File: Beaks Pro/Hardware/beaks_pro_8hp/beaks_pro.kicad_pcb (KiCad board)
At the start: 2 copper layers, 40 x 110 mm, 138 parts, among them J1 Pins_02x10_P2.54mm_TH, J11 out1, J12 out2, J13 Eurorack Power, J14 Pins_02x10_P2.54mm_TH, J2 Pins_02x10_P2.54mm_TH, J3 CV1, J4 CV2, J5 CV3, J6 CV4, J7 in1, J8 in2, J9 Pins_02x10_P2.54mm_TH, Q1 2N3904, Q2 2N3904, SW2 SW_Dual, SW3 SW_Mode, SW5 SW_ML6, SW6 SW_ML6, U1 TL072CP, U2 MCP6002-I-P, U3 TL072CP, U4 MCP6002-I-P, U5 TL074, U6 LM4040LP-10, U7 L78L05_TO92, U8 Bluepill, U9 TL072CP

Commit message: Layout done on 8HP SMT version
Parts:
- removed D10: 3.6, Diode_THT:D_DO-35_SOD27_P7.62mm_Horizontal
- added C25: 100n, Capacitor_SMD:C_0603_1608Metric_Pad1.08x0.95mm_HandSolder, F.Cu at (170.5, 74.0)
- added C26: 100n, Capacitor_SMD:C_0603_1608Metric_Pad1.08x0.95mm_HandSolder, F.Cu at (187.5, 101.4)
- added DZ1: ZMM3V6, PCM_Diode_SMD_AKL:D_SOD-323, F.Cu at (154.0, 138.0)
- C1, C13, C16, C2, C20, C22, C24, C5, C6: footprint Capacitor_THT:C_Rect_L10.0mm_W4.0mm_P7.50mm_MKS4 -> Capacitor_SMD:C_0603_1608Metric_Pad1.08x0.95mm_HandSolder
- C10, C11, C12, C14, C15, C3, C4, C7, C8, C9: footprint Capacitor_THT:C_Disc_D3.4mm_W2.1mm_P2.50mm -> Capacitor_SMD:C_0603_1608Metric_Pad1.08x0.95mm_HandSolder
- C17, C18, C19: value 10u -> 22uF; footprint Capacitor_THT:CP_Radial_D8.0mm_P3.50mm -> Capacitor_SMD:C_1206_3216Metric_Pad1.33x1.80mm_HandSolder
- C21: value 0,33u -> 22uF; footprint Capacitor_THT:C_Rect_L10.0mm_W4.0mm_P7.50mm_MKS4 -> Capacitor_SMD:C_1206_3216Metric_Pad1.33x1.80mm_HandSolder
- C23: value 100n -> 22uF; footprint Capacitor_THT:C_Rect_L10.0mm_W4.0mm_P7.50mm_MKS4 -> Capacitor_SMD:C_1206_3216Metric_Pad1.33x1.80mm_HandSolder
- D11, D8, D9: value 1N5817 -> B140HW-7; footprint Diode_THT:D_DO-41_SOD81_P10.16mm_Horizontal -> Diode_SMD:D_SOD-123
- J1: value Pins_02x10_P2.54mm_TH -> Conn_02x08_Odd_Even; footprint Connector_PinHeader_2.54mm:PinHeader_2x10_P2.54mm_Vertical -> Connector_PinSocket_2.54mm:PinSocket_2x08_P2.54mm_Vertical
- J13, U8: moved to B.Cu
- J14: value Pins_02x10_P2.54mm_TH -> Conn_02x12_Odd_Even; footprint Connector_PinHeader_2.54mm:PinHeader_2x10_P2.54mm_Vertical -> Connector_PinSocket_2.54mm:PinSocket_2x12_P2.54mm_Vertical
- J2: value Pins_02x10_P2.54mm_TH -> Conn_02x12_Odd_Even; footprint Connector_PinSocket_2.54mm:PinSocket_2x10_P2.54mm_Vertical -> Connector_PinHeader_2.54mm:PinHeader_2x12_P2.54mm_Vertical
- J9: value Pins_02x10_P2.54mm_TH -> Conn_02x08_Odd_Even; footprint Connector_PinSocket_2.54mm:PinSocket_2x10_P2.54mm_Vertical -> Connector_PinHeader_2.54mm:PinHeader_2x08_P2.54mm_Vertical
- Q1, Q2: value 2N3904 -> S8050 J3Y; footprint Package_TO_SOT_THT:TO-92_Inline_Wide -> PCM_Package_TO_SOT_SMD_AKL:SOT-23
- R1, R10, R11, R12, R13, R14, R15, R16, R17, R18, R19, R2, R20, R21, R22, R23, R24, R25, R26, R27, R28, R29, R3, R30, R31, R32, R33, R34, R35, R36, R37, R38, R39, R4, R40, R41, R42, R43, R44, R45, R46, R47, R48, R49, R5, R50, R51, R52, R53, R54, R55, R56, R57, R58, R59, R6, R60, R61, R62, R63, R64, R65, R7, R8, R9: footprint Resistor_THT:R_Axial_DIN0207_L6.3mm_D2.5mm_P7.62mm_Horizontal -> Resistor_SMD:R_0603_1608Metric_Pad0.98x0.95mm_HandSolder
- U1, U3, U9: value TL072CP -> TL072CD; footprint PCM_Package_DIP_AKL:DIP-8_W7.62mm_Socket_LongPads -> PCM_Package_SO_AKL:SO-8_3.9x4.9mm_P1.27mm
- U2, U4: value MCP6002-I-P -> MCP6002-I-SN; footprint PCM_Package_DIP_AKL:DIP-8_W7.62mm_Socket_LongPads -> PCM_Package_SO_AKL:SO-8_3.9x4.9mm_P1.27mm
- U5: value TL074 -> TL074CD; footprint Package_DIP:DIP-14_W7.62mm_Socket_LongPads -> PCM_Package_SO_AKL:SOIC-14_3.9x8.7mm_P1.27mm
- U6: value LM4040LP-10 -> LM4040DBZ-10; footprint Package_TO_SOT_THT:TO-92_Inline_Wide -> Package_TO_SOT_SMD:SOT-23
- U7: value L78L05_TO92 -> AMS1117-5.0; footprint PCM_Package_TO_SOT_THT_AKL:TO-92L_Inline_Wide -> Package_TO_SOT_SMD:SOT-223-3_TabPin2
- moved H1 381.5 mm to (173.0, 43.5)
- moved C24 345.8 mm to (158.0, 111.0), turned to 90 degrees
- moved J1 344.6 mm to (174.0, 98.0)
- moved U9 342.4 mm to (162.0, 111.5), turned to -90 degrees
- moved J14 341.0 mm to (184.0, 122.5), turned to -90 degrees
- moved R59 336.6 mm to (156.0, 112.0), turned to 90 degrees
- moved R63 336.6 mm to (156.0, 126.6), turned to 180 degrees
- moved R58 335.8 mm to (157.1, 115.0)
- moved R60 335.6 mm to (157.0, 117.0)
- moved R62 333.3 mm to (159.4, 126.6), turned to 180 degrees
- moved R64 333.0 mm to (159.5, 128.6), turned to 180 degrees
- moved R61 332.1 mm to (160.5, 117.0)
- moved R65 329.6 mm to (163.5, 106.5)
- moved R43 325.8 mm to (167.5, 113.0), turned to 180 degrees
- moved R44 325.6 mm to (167.5, 115.0), turned to 180 degrees
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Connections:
- C13 pad 2: -12V -> GND
- C21 pad 1: +12V -> +5V
- C23 pad 1: +5V -> +12V
- C5 pad 2: -12V -> GND
- J1 pad 1: /PRE_ATV_OUT1 -> /LED_SALIDA_1
- J1 pad 10: /SW_TRIG1 -> GND
- J1 pad 11: /LED2 -> /LED4
- J1 pad 12: /SW_TRIG2 -> GND
- J1 pad 13: /LED3 -> /LED5
- J1 pad 14: GND -> /OUT1
- J1 pad 15: /LED4 -> GND
- J1 pad 16: GND -> /OUT2
- J1 pad 2: /PRE_ATV_OUT2 -> /SW_DUAL
- J1 pad 3: /OUT1_ATVPOT -> /LED_SALIDA_2
- J1 pad 4: /OUT2_ATVPOT -> /SW_MODE
- J1 pad 5: /LED_SALIDA_1 -> /LED1
- J1 pad 6: /SW_DUAL -> /SW_TRIG1
- J1 pad 7: /LED_SALIDA_2 -> /LED2
- J1 pad 8: /SW_MODE -> /SW_TRIG2
- J1 pad 9: /LED1 -> /LED3
- J2 pad 1: GND -> GND1
- J2 pad 10: /Front PCB/CV2_JACK -> /Front PCB/TRIG_2
- J2 pad 11: /Front PCB/CV4_POT -> /Front PCB/CV2_ATVPOT
- J2 pad 12: /Front PCB/CV2_ATVPOT -> /Front PCB/CV4_POT
- J2 pad 13: /Front PCB/CV4_ATVPOT -> /Front PCB/CV2_POT
- J2 pad 14: /Front PCB/CV2_POT -> /Front PCB/CV4_ATVPOT
- J2 pad 15: /Front PCB/CV4_JACK -> /Front PCB/CV3_JACK
- J2 pad 16: /Front PCB/CV3_JACK -> /Front PCB/CV4_JACK
- J2 pad 17: /Front PCB/CV3_POT -> /Front PCB/CV3_ATVPOT
- J2 pad 18: /Front PCB/CV3_ATVPOT -> /Front PCB/CV3_POT
- J2 pad 19: GND -> GND1
- J2 pad 2: GND -> GND1
- J2 pad 20: GND -> GND1
- J2 pad 3: /Front PCB/-10V_REF -> /Front PCB/CV1_JACK
- J2 pad 4: /Front PCB/CV1_JACK -> /Front PCB/-10V_REF
- J2 pad 5: GND -> /Front PCB/CV1_ATVPOT
- J2 pad 6: /Front PCB/CV1_ATVPOT -> GND1
- J2 pad 7: /Front PCB/TRIG_1 -> /Front PCB/CV1_POT
- J2 pad 8: /Front PCB/CV1_POT -> /Front PCB/TRIG_1
- J2 pad 9: /Front PCB/TRIG_2 -> /Front PCB/CV2_JACK
- J9 pad 1: /Front PCB/PRE_ATV_OUT2 -> /Front PCB/LED_SALIDA_1
- J9 pad 10: /Front PCB/LED1 -> GND1
- J9 pad 11: /Front PCB/SW_TRIG2 -> /Front PCB/LED4
- J9 pad 12: /Front PCB/LED2 -> GND1
- J9 pad 13: GND -> /Front PCB/LED5
- J9 pad 14: /Front PCB/LED3 -> /Front PCB/OUT1
- J9 pad 15: GND -> GND1
- J9 pad 16: /Front PCB/LED4 -> /Front PCB/OUT2
- J9 pad 2: /Front PCB/PRE_ATV_OUT1 -> /Front PCB/SW_DUAL
- J9 pad 3: /Front PCB/OUT2_ATVPOT -> /Front PCB/LED_SALIDA_2
- J9 pad 4: /Front PCB/OUT1_ATVPOT -> /Front PCB/SW_MODE
- J9 pad 5: /Front PCB/SW_DUAL -> /Front PCB/LED1
- J9 pad 6: /Front PCB/LED_SALIDA_1 -> /Front PCB/SW_TRIG1
- J9 pad 7: /Front PCB/SW_MODE -> /Front PCB/LED2
- J9 pad 8: /Front PCB/LED_SALIDA_2 -> /Front PCB/SW_TRIG2
- J9 pad 9: /Front PCB/SW_TRIG1 -> /Front PCB/LED3
- Q1 pad 1: GND -> Net-(Q1-B)
- Q1 pad 2: Net-(Q1-B) -> GND
- Q2 pad 1: GND -> Net-(Q2-B)
- Q2 pad 2: Net-(Q2-B) -> GND
- U6 pad 1: unconnected-(U6-NC-Pad1) -> GND
- U6 pad 2: GND -> /-10V_REF
- U6 pad 3: /-10V_REF -> unconnected-(U6-NC-Pad3)
- U7 pad 1: +5V -> GND
- U7 pad 2: GND -> +5V
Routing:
- net -12V: track 0.00 -> 284.4 mm, vias 0 -> 6
- net +12V: track 0.00 -> 249.9 mm, vias 0 -> 6
- net /Front PCB/CV1_JACK: track 0.00 -> 164.2 mm
- net /Output/-3V6_REF: track 0.00 -> 148.5 mm, vias 0 -> 3
- net /Front PCB/CV3_ATVPOT: track 0.00 -> 125.7 mm
- net /Front PCB/CV4_JACK: track 0.00 -> 120.9 mm, vias 0 -> 1
- net /PRE_ATV_OUT2: track 0.00 -> 109.2 mm, vias 0 -> 1
- net Net-(U4A--): track 0.00 -> 99.6 mm, vias 0 -> 3
- net +3V3: track 0.00 -> 94.2 mm, vias 0 -> 4
- net /Front PCB/CV4_ATVPOT: track 0.00 -> 94.0 mm
- net /PRE_ATV_OUT1: track 0.00 -> 93.2 mm
- net /Front PCB/CV4_POT: track 0.00 -> 87.7 mm
- net /Front PCB/-10V_REF: track 0.00 -> 87.0 mm
- net /Front PCB/CV3_JACK: track 0.00 -> 83.7 mm
- net Net-(U2A--): track 0.00 -> 80.5 mm, vias 0 -> 2
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- added copper zone on B.Cu, net GND
- added copper zone on F.Cu, net GND
- added copper zone on B.Cu, net GND1
- added copper zone on F.Cu, net GND1
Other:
- board size 40 x 110 mm -> 90 x 110 mm
- board text added: "**"

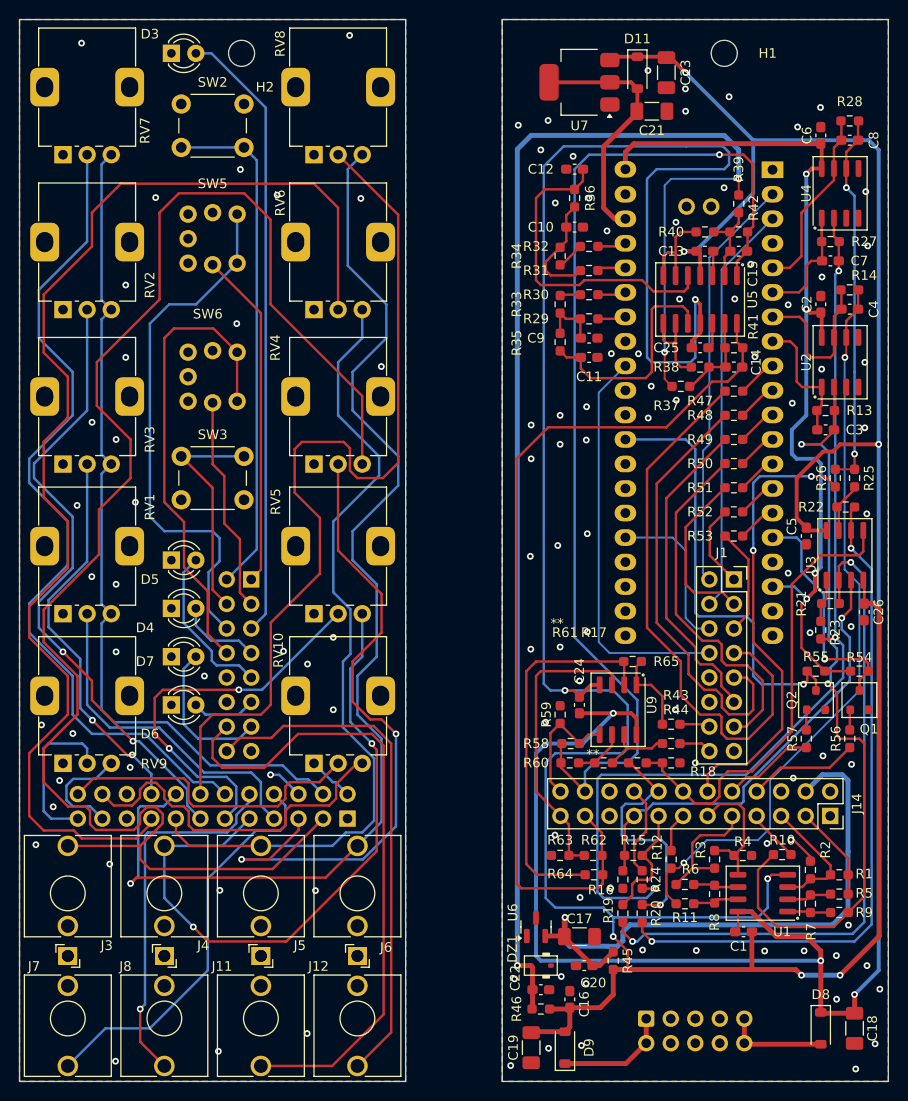
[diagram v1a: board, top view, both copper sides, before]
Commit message: Split 8HP design up in separate files, for SMT export. Add step file export
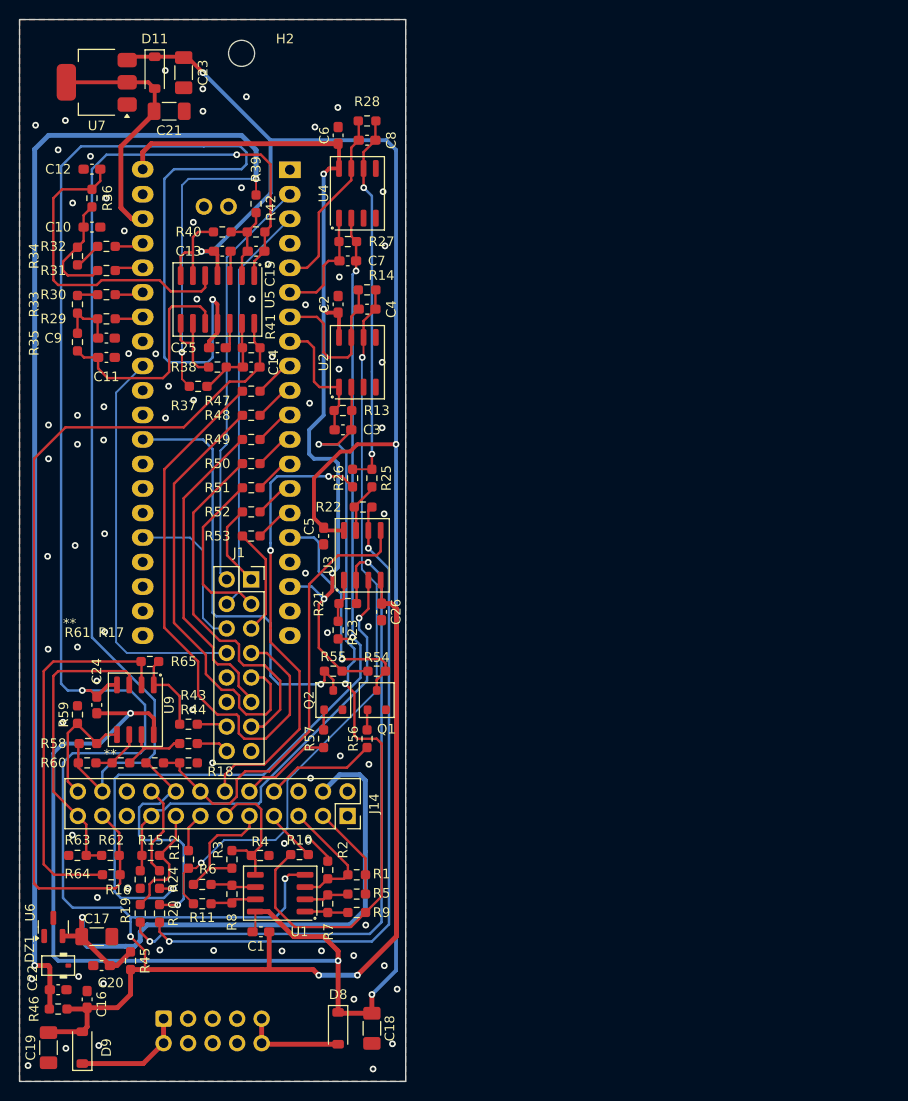
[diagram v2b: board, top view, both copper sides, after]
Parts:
- removed D3, D4, D5, D6, D7: LED, LED_THT:LED_D3.0mm
- removed H1: MountingHole, MountingHole:MountingHole_2.7mm_M2.5
- removed J11: out1, Library:Jack_3.5mm_QingPu_WQP-PJ398SM_Vertical_CircularHoles_3D
- removed J12: out2, Library:Jack_3.5mm_QingPu_WQP-PJ398SM_Vertical_CircularHoles_3D
- removed J2: Conn_02x12_Odd_Even, Connector_PinHeader_2.54mm:PinHeader_2x12_P2.54mm_Vertical
- removed J3: CV1, Library:Jack_3.5mm_QingPu_WQP-PJ398SM_Vertical_CircularHoles_3D
- removed J4: CV2, Library:Jack_3.5mm_QingPu_WQP-PJ398SM_Vertical_CircularHoles_3D
- removed J5: CV3, Library:Jack_3.5mm_QingPu_WQP-PJ398SM_Vertical_CircularHoles_3D
- removed J6: CV4, Library:Jack_3.5mm_QingPu_WQP-PJ398SM_Vertical_CircularHoles_3D
- removed J7: in1, Library:Jack_3.5mm_QingPu_WQP-PJ398SM_Vertical_CircularHoles_3D
- removed J8: in2, Library:Jack_3.5mm_QingPu_WQP-PJ398SM_Vertical_CircularHoles_3D
- removed J9: Conn_02x08_Odd_Even, Connector_PinHeader_2.54mm:PinHeader_2x08_P2.54mm_Vertical
- removed RV1, RV2, RV3, RV7: B10k, Library:Potentiometer_Alps_RK09K_Single_Vertical_DSHAFT
- removed RV10, RV4, RV5, RV6, RV8, RV9: B100k, Library:Potentiometer_Alps_RK09K_Single_Vertical
- removed SW2: SW_Dual, Button_Switch_THT:SW_PUSH_6mm_H13mm
- removed SW3: SW_Mode, Button_Switch_THT:SW_PUSH_6mm_H13mm
- removed SW5, SW6: SW_ML6, Library:ML6-H2T2GQA
- moved R11 50.0 mm to (118.9, 131.6)
- moved R4 50.0 mm to (124.9, 126.6)
- moved R6 50.0 mm to (118.9, 129.6)
- moved C1 50.0 mm to (125.0, 134.5)
- moved C10 50.0 mm to (107.5, 61.5)
- moved C11 50.0 mm to (109.0, 75.0)
- moved C12 50.0 mm to (107.5, 55.5)
- moved C13 50.0 mm to (121.0, 64.0)
- moved C14 50.0 mm to (124.0, 76.0)
- moved C15 50.0 mm to (124.5, 64.0)
- moved C16 50.0 mm to (107.0, 141.5)
- moved C17 50.0 mm to (108.0, 135.0)
- moved C18 50.0 mm to (136.5, 144.5)
- moved C19 50.0 mm to (103.0, 146.5)
- moved C2 50.0 mm to (133.0, 69.5)
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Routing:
- net /Front PCB/CV1_JACK: track 164.2 -> 0.00 mm
- net /Front PCB/CV3_ATVPOT: track 125.7 -> 0.00 mm
- net /Front PCB/CV4_JACK: track 120.9 -> 0.00 mm, vias 1 -> 0
- net /Front PCB/CV4_ATVPOT: track 94.0 -> 0.00 mm
- net /Front PCB/CV4_POT: track 87.7 -> 0.00 mm
- net /Front PCB/-10V_REF: track 87.0 -> 0.00 mm
- net /Front PCB/CV3_JACK: track 83.7 -> 0.00 mm
- net /Front PCB/CV2_JACK: track 69.4 -> 0.00 mm, vias 2 -> 0
- net /Front PCB/CV1_ATVPOT: track 68.9 -> 0.00 mm, vias 2 -> 0
- net /Front PCB/OUT1: track 66.7 -> 0.00 mm
- net /Front PCB/CV2_POT: track 65.4 -> 0.00 mm, vias 2 -> 0
- net /Front PCB/LED1: track 64.1 -> 0.00 mm
- net /Front PCB/SW_TRIG1: track 55.5 -> 0.00 mm
- net /Front PCB/OUT2: track 53.7 -> 0.00 mm
- net /Front PCB/SW_DUAL: track 53.1 -> 0.00 mm
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- removed copper zone on B.Cu, net GND1
- removed copper zone on F.Cu, net GND1
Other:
- board size 90 x 110 mm -> 40 x 110 mm
- board text added: "Design by Sluisbrinkie"
